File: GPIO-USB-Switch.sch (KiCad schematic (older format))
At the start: 14 parts, among them J1 Jetson_GPIO_OUT, J2 USB3.0-Type-A_Male, J3 USB3.0-Type-A_Female, Q1 BSS138, Q2 DMG2301L

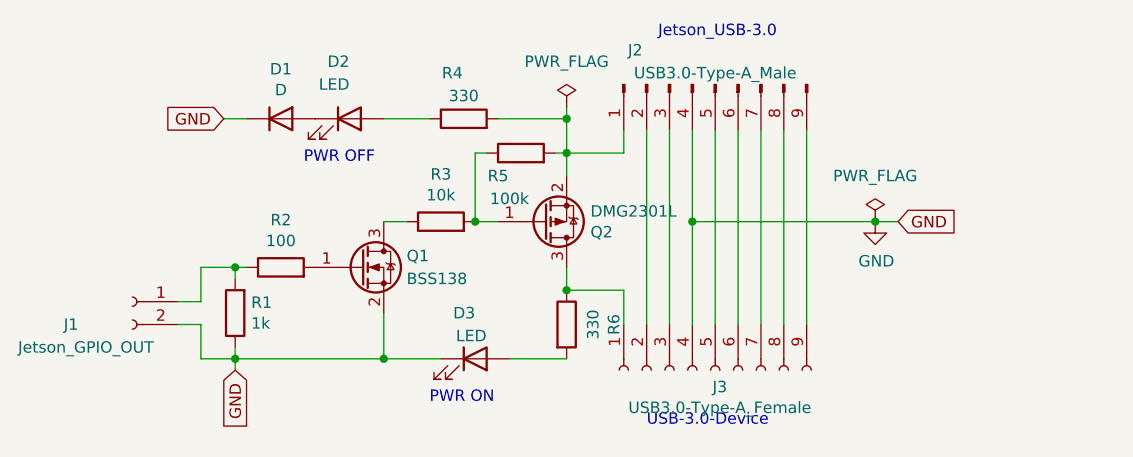
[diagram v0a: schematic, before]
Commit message: added local labels for USB connectors
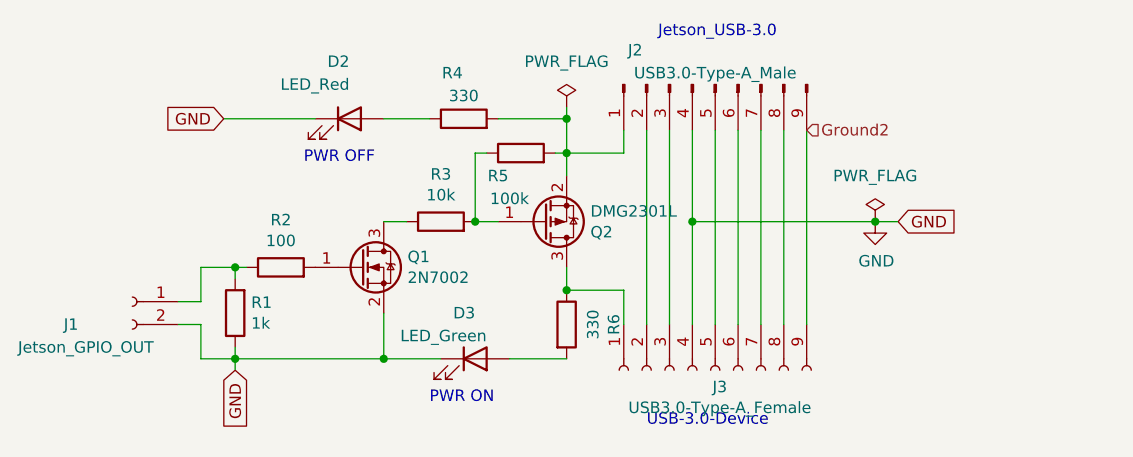
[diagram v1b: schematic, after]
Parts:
- removed D1: D, Diode_SMD:D_0805_2012Metric_Pad1.15x1.40mm_HandSolder, symbol Device:D
- removed Q1: BSS138, Package_TO_SOT_SMD:SOT-23, symbol Transistor_FET:BSS138
- added Q1: 2N7002, Package_TO_SOT_SMD:SOT-23, symbol Transistor_FET:2N7002
- D2: value LED -> LED_Red; footprint LED_SMD:LED_0805_2012Metric_Pad1.15x1.40mm_HandSolder -> LED_SMD:LED_0603_1608Metric_Pad1.05x0.95mm_HandSolder
- D3: value LED -> LED_Green; footprint LED_SMD:LED_0805_2012Metric_Pad1.15x1.40mm_HandSolder -> LED_SMD:LED_0603_1608Metric_Pad1.05x0.95mm_HandSolder
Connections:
- net GND: now also D2.1 (K), Q1.2 (S)
- net at R2.2: now also Q1.1 (G)
- net Ground2: now reaches J2.9 (Pin_9), J3.9 (Pin_9)
- net at R3.1: now also Q1.3 (D)
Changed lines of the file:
@@
 	0    -1   1    0
-$EndComp
-$Comp
-L Transistor_FET:BSS138 Q1
-U 1 1 60635E6E
-P 3100 3200
-F 0 "Q1" H 3300 3250 50  0000 L CNN
-F 1 "BSS138" H 3300 3150 50  0000 L CNN
-F 2 "Package_TO_SOT_SMD:SOT-23" H 3300 3125 50  0001 L CIN
-F 3 "https://www.fairchildsemi.com/datasheets/BS/BSS138.pdf" H 3100 3200 50  0001 L CNN
-	1    3100 3200
-	1    0    0    -1
 $EndComp
 Wire Wire Line
@@
 P 3600 3600
 F 0 "D3" H 3600 3800 50  0000 R CNN
-F 1 "LED" H 3650 3700 50  0000 R CNN
-F 2 "LED_SMD:LED_0805_2012Metric_Pad1.15x1.40mm_HandSolder" H 3600 3600 50  0001 C CNN
+F 1 "LED_Green" H 3650 3700 50  0000 R CNN
+F 2 "LED_SMD:LED_0603_1608Metric_Pad1.05x0.95mm_HandSolder" H 3600 3600 50  0001 C CNN
 F 3 "~" H 3600 3600 50  0001 C CNN
 	1    3600 3600
@@
 P 3050 2550
 F 0 "D2" H 3050 2800 50  0000 R CNN
-F 1 "LED" H 3050 2700 50  0000 R CNN
-F 2 "LED_SMD:LED_0805_2012Metric_Pad1.15x1.40mm_HandSolder" H 3050 2550 50  0001 C CNN
+F 1 "LED_Red" H 3050 2700 50  0000 R CNN
+F 2 "LED_SMD:LED_0603_1608Metric_Pad1.05x0.95mm_HandSolder" H 3050 2550 50  0001 C CNN
 F 3 "~" H 3050 2550 50  0001 C CNN
 	1    3050 2550
@@
 Text GLabel 2500 2550 0    50   Input ~ 0
 GND
-$Comp
-L Device:D D1
-U 1 1 6064ACF0
-P 2750 2550
-F 0 "D1" H 2750 2767 50  0000 C CNN
-F 1 "D" H 2750 2676 50  0000 C CNN
-F 2 "Diode_SMD:D_0805_2012Metric_Pad1.15x1.40mm_HandSolder" H 2750 2550 50  0001 C CNN
-F 3 "~" H 2750 2550 50  0001 C CNN
-	1    2750 2550
-	1    0    0    -1
-$EndComp
-Wire Wire Line
-	2600 2550 2500 2550
 Wire Wire Line
 	5050 2600 5050 3450
@@
 Wire Wire Line
 	4950 2600 4950 3450
+$Comp
+L Transistor_FET:2N7002 Q1
+U 1 1 609D6A8D
+P 3100 3200
+F 0 "Q1" H 3304 3246 50  0000 L CNN
+F 1 "2N7002" H 3304 3155 50  0000 L CNN
+F 2 "Package_TO_SOT_SMD:SOT-23" H 3300 3125 50  0001 L CIN
+F 3 "https://www.fairchildsemi.com/datasheets/2N/2N7002.pdf" H 3100 3200 50  0001 L CNN
+	1    3100 3200
+	1    0    0    -1
+$EndComp
+Wire Wire Line
+	2500 2550 2900 2550
+Text HLabel 5050 2600 2    50   Input ~ 0
+Ground2
 $EndSCHEMATC

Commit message: finished 4-layer layout!
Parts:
- D2, D3: footprint LED_SMD:LED_0603_1608Metric_Pad1.05x0.95mm_HandSolder -> LED_SMD:LED_0603_1608Metric
- J1: value Jetson_GPIO_OUT -> GPIO_OUT
- R1, R2, R3, R4, R5, R6: footprint Resistor_SMD:R_0805_2012Metric_Pad1.20x1.40mm_HandSolder -> Resistor_SMD:R_0603_1608Metric
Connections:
- net D-: now reaches J2.2 (Pin_2), J3.2 (Pin_2)
- net D+: now reaches J2.3 (Pin_3), J3.3 (Pin_3)
- net StdA_SSRX-: now reaches J2.5 (Pin_5), J3.5 (Pin_5)
- net StdA_SSRX+: now reaches J2.6 (Pin_6), J3.6 (Pin_6)
- net StdA_SSTX-: now reaches J2.8 (Pin_8), J3.8 (Pin_8)
- net VBUS: now reaches J2.1 (Pin_1), Q2.2 (S), R4.2, R5.2
- net Ground2 renamed StdA_SSTX+
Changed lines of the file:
@@
 F 0 "R2" V 2957 3200 50  0000 C CNN
 F 1 "100" V 2866 3200 50  0000 C CNN
-F 2 "Resistor_SMD:R_0805_2012Metric_Pad1.20x1.40mm_HandSolder" V 2680 3200 50  0001 C CNN
+F 2 "Resistor_SMD:R_0603_1608Metric" V 2680 3200 50  0001 C CNN
 F 3 "~" H 2750 3200 50  0001 C CNN
 	1    2750 3200
@@
 F 0 "R1" H 2480 3354 50  0000 R CNN
 F 1 "1k" H 2480 3445 50  0000 R CNN
-F 2 "Resistor_SMD:R_0805_2012Metric_Pad1.20x1.40mm_HandSolder" V 2480 3400 50  0001 C CNN
+F 2 "Resistor_SMD:R_0603_1608Metric" V 2480 3400 50  0001 C CNN
 F 3 "~" H 2550 3400 50  0001 C CNN
 	1    2550 3400
@@
 F 0 "R3" V 3657 3000 50  0000 C CNN
 F 1 "10k" V 3566 3000 50  0000 C CNN
-F 2 "Resistor_SMD:R_0805_2012Metric_Pad1.20x1.40mm_HandSolder" V 3380 3000 50  0001 C CNN
+F 2 "Resistor_SMD:R_0603_1608Metric" V 3380 3000 50  0001 C CNN
 F 3 "~" H 3450 3000 50  0001 C CNN
 	1    3450 3000
@@
 F 0 "R5" V 3700 2800 50  0000 C CNN
 F 1 "100k" V 3600 2750 50  0000 C CNN
-F 2 "Resistor_SMD:R_0805_2012Metric_Pad1.20x1.40mm_HandSolder" V 3730 2700 50  0001 C CNN
+F 2 "Resistor_SMD:R_0603_1608Metric" V 3730 2700 50  0001 C CNN
 F 3 "~" H 3800 2700 50  0001 C CNN
 	1    3800 2700
@@
 L power:PWR_FLAG #FLG02
 U 1 1 6068CE02
-P 5350 3000
-F 0 "#FLG02" H 5350 3075 50  0001 C CNN
-F 1 "PWR_FLAG" H 5350 3200 50  0000 C CNN
-F 2 "" H 5350 3000 50  0001 C CNN
-F 3 "~" H 5350 3000 50  0001 C CNN
-	1    5350 3000
+P 6000 3000
+F 0 "#FLG02" H 6000 3075 50  0001 C CNN
+F 1 "PWR_FLAG" H 6000 3200 50  0000 C CNN
+F 2 "" H 6000 3000 50  0001 C CNN
+F 3 "~" H 6000 3000 50  0001 C CNN
+	1    6000 3000
 	1    0    0    -1
 $EndComp
@@
 L power:GND #PWR01
 U 1 1 60640792
-P 5350 3000
-F 0 "#PWR01" H 5350 2750 50  0001 C CNN
-F 1 "GND" H 5355 2827 50  0000 C CNN
-F 2 "" H 5350 3000 50  0001 C CNN
-F 3 "" H 5350 3000 50  0001 C CNN
-	1    5350 3000
-	1    0    0    -1
-$EndComp
-Wire Wire Line
-	4550 2600 4550 3000
-Connection ~ 4550 3000
-Connection ~ 5350 3000
-Wire Wire Line
-	5350 3000 4550 3000
+P 6000 3000
+F 0 "#PWR01" H 6000 2750 50  0001 C CNN
+F 1 "GND" H 6005 2827 50  0000 C CNN
+F 2 "" H 6000 3000 50  0001 C CNN
+F 3 "" H 6000 3000 50  0001 C CNN
+	1    6000 3000
+	1    0    0    -1
+$EndComp
+Connection ~ 6000 3000
 Connection ~ 2550 3200
-Text GLabel 5450 3000 2    50   Input ~ 0
+Text GLabel 6100 3000 2    50   Input ~ 0
 GND
 Wire Wire Line
-	5350 3000 5450 3000
+	6000 3000 6100 3000
 Text GLabel 2550 3650 3    50   Input ~ 0
 GND
@@
 P 2100 3350
 F 0 "J1" H 2400 3250 50  0000 R CNN
-F 1 "Jetson_GPIO_OUT" H 2600 3150 50  0000 R CNN
+F 1 "GPIO_OUT" H 2600 3150 50  0000 R CNN
 F 2 "Connector_JST:JST_XH_B2B-XH-A_1x02_P2.50mm_Vertical" H 2100 3350 50  0001 C CNN
 F 3 "~" H 2100 3350 50  0001 C CNN
@@
 U 1 1 606A6199
 P 3900 3000
-F 0 "Q2" H 4104 3046 50  0000 L CNN
-F 1 "DMG2301L" H 4104 2955 50  0000 L CNN
+F 0 "Q2" H 4100 3100 50  0000 L CNN
+F 1 "DMG2301L" H 4100 3000 50  0000 L CNN
 F 2 "Package_TO_SOT_SMD:SOT-23" H 4100 2925 50  0001 L CIN
 F 3 "https://www.diodes.com/assets/Datasheets/DMG2301L.pdf" H 3900 3000 50  0001 L CNN
@@
 F 0 "R6" V 4207 3450 50  0000 C CNN
 F 1 "330" V 4116 3450 50  0000 C CNN
-F 2 "Resistor_SMD:R_0805_2012Metric_Pad1.20x1.40mm_HandSolder" V 3930 3450 50  0001 C CNN
+F 2 "Resistor_SMD:R_0603_1608Metric" V 3930 3450 50  0001 C CNN
 F 3 "~" H 4000 3450 50  0001 C CNN
 	1    4000 3450
@@
 F 0 "D3" H 3600 3800 50  0000 R CNN
 F 1 "LED_Green" H 3650 3700 50  0000 R CNN
-F 2 "LED_SMD:LED_0603_1608Metric_Pad1.05x0.95mm_HandSolder" H 3600 3600 50  0001 C CNN
+F 2 "LED_SMD:LED_0603_1608Metric" H 3600 3600 50  0001 C CNN
 F 3 "~" H 3600 3600 50  0001 C CNN
 	1    3600 3600
@@
 F 0 "R4" V 3750 2600 50  0000 C CNN
 F 1 "330" V 3650 2550 50  0000 C CNN
-F 2 "Resistor_SMD:R_0805_2012Metric_Pad1.20x1.40mm_HandSolder" V 3480 2550 50  0001 C CNN
+F 2 "Resistor_SMD:R_0603_1608Metric" V 3480 2550 50  0001 C CNN
 F 3 "~" H 3550 2550 50  0001 C CNN
 	1    3550 2550
@@
 F 0 "D2" H 3050 2800 50  0000 R CNN
 F 1 "LED_Red" H 3050 2700 50  0000 R CNN
-F 2 "LED_SMD:LED_0603_1608Metric_Pad1.05x0.95mm_HandSolder" H 3050 2550 50  0001 C CNN
+F 2 "LED_SMD:LED_0603_1608Metric" H 3050 2550 50  0001 C CNN
 F 3 "~" H 3050 2550 50  0001 C CNN
 	1    3050 2550
@@
 GND
 Wire Wire Line
-	5050 2600 5050 3450
-Wire Wire Line
 	4250 3300 4250 3450
 Wire Wire Line
-	4350 2600 4350 3450
-Wire Wire Line
-	4450 2600 4450 3450
-Wire Wire Line
-	4550 3000 4550 3450
-Wire Wire Line
-	4650 2600 4650 3450
-Wire Wire Line
-	4750 2600 4750 3450
+	4350 2600 4350 2750
+Wire Wire Line
+	4450 2600 4450 2850
+Wire Wire Line
+	4750 2600 4750 2850
 Wire Wire Line
 	4850 2600 4850 3450
 Wire Wire Line
-	4950 2600 4950 3450
+	4950 2600 4950 3300
 $Comp
 L Transistor_FET:2N7002 Q1
@@
 Wire Wire Line
 	2500 2550 2900 2550
-Text HLabel 5050 2600 2    50   Input ~ 0
-Ground2
+Wire Wire Line
+	3950 2500 4000 2500
+Connection ~ 4000 2500
+Text GLabel 3950 2500 0    50   Input ~ 0
+VBUS
+Text GLabel 4300 2750 0    50   Input ~ 0
+D-
+Text GLabel 4300 2850 0    50   Input ~ 0
+D+
+Wire Wire Line
+	4300 2750 4350 2750
+Connection ~ 4350 2750
+Wire Wire Line
+	4350 2750 4350 3450
+Wire Wire Line
+	4300 2850 4450 2850
+Connection ~ 4450 2850
+Wire Wire Line
+	4450 2850 4450 3450
+Text GLabel 5200 3300 2    50   Input ~ 0
+StdA_SSTX-
+Text GLabel 5200 3400 2    50   Input ~ 0
+StdA_SSTX+
+Wire Wire Line
+	5050 2600 5050 3400
+Wire Wire Line
+	6000 3000 4550 3000
+Wire Wire Line
+	4550 2600 4550 3000
+Connection ~ 4550 3000
+Wire Wire Line
+	4550 3000 4550 3450
+Wire Wire Line
+	5200 3300 4950 3300
+Connection ~ 4950 3300
+Wire Wire Line
+	4950 3300 4950 3450
+Wire Wire Line
+	5200 3400 5050 3400
+Connection ~ 5050 3400
+Wire Wire Line
+	5050 3400 5050 3450
+Text GLabel 5200 2750 2    50   Input ~ 0
+StdA_SSRX-
+Text GLabel 5200 2850 2    50   Input ~ 0
+StdA_SSRX+
+Wire Wire Line
+	5200 2750 4650 2750
+Wire Wire Line
+	4650 2600 4650 2750
+Connection ~ 4650 2750
+Wire Wire Line
+	4650 2750 4650 3450
+Wire Wire Line
+	4750 2850 5200 2850
+Connection ~ 4750 2850
+Wire Wire Line
+	4750 2850 4750 3450
 $EndSCHEMATC
